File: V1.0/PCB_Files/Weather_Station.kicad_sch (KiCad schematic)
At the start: 45 parts, among them J1 N091-2832TSWFG02-H14, J2 USB_B_Micro, J3 Conn_01x04_Pin, J4 Conn_01x04_Pin, J5 Conn_01x06_Pin, U1 STM32F103C8T6, U2 HDC1080DMBR, U3 AMS1117-3.3, U5 SRV05-4, Y1 X322516MLB4SI

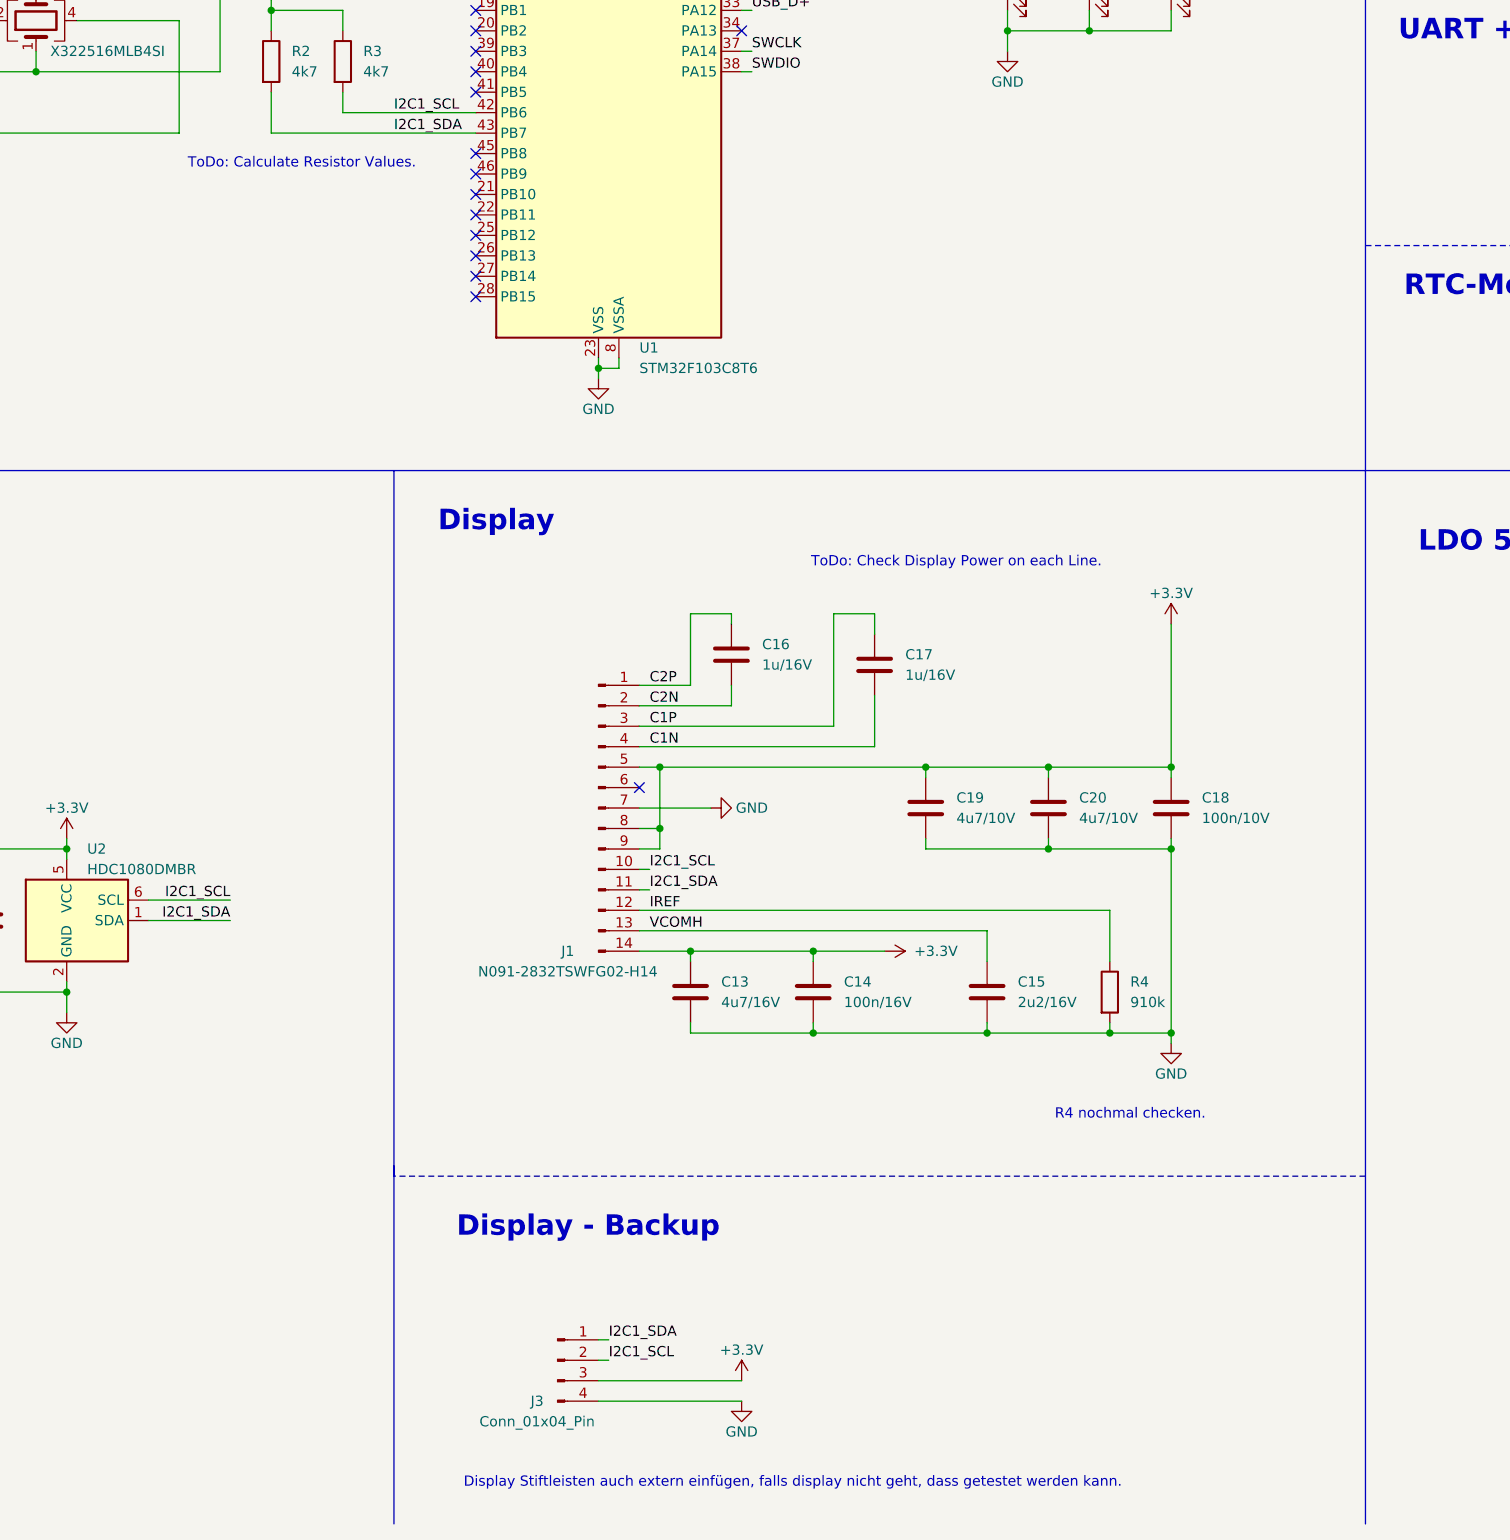
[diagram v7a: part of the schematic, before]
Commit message: Decided to not go with the display. Added Step file for display.
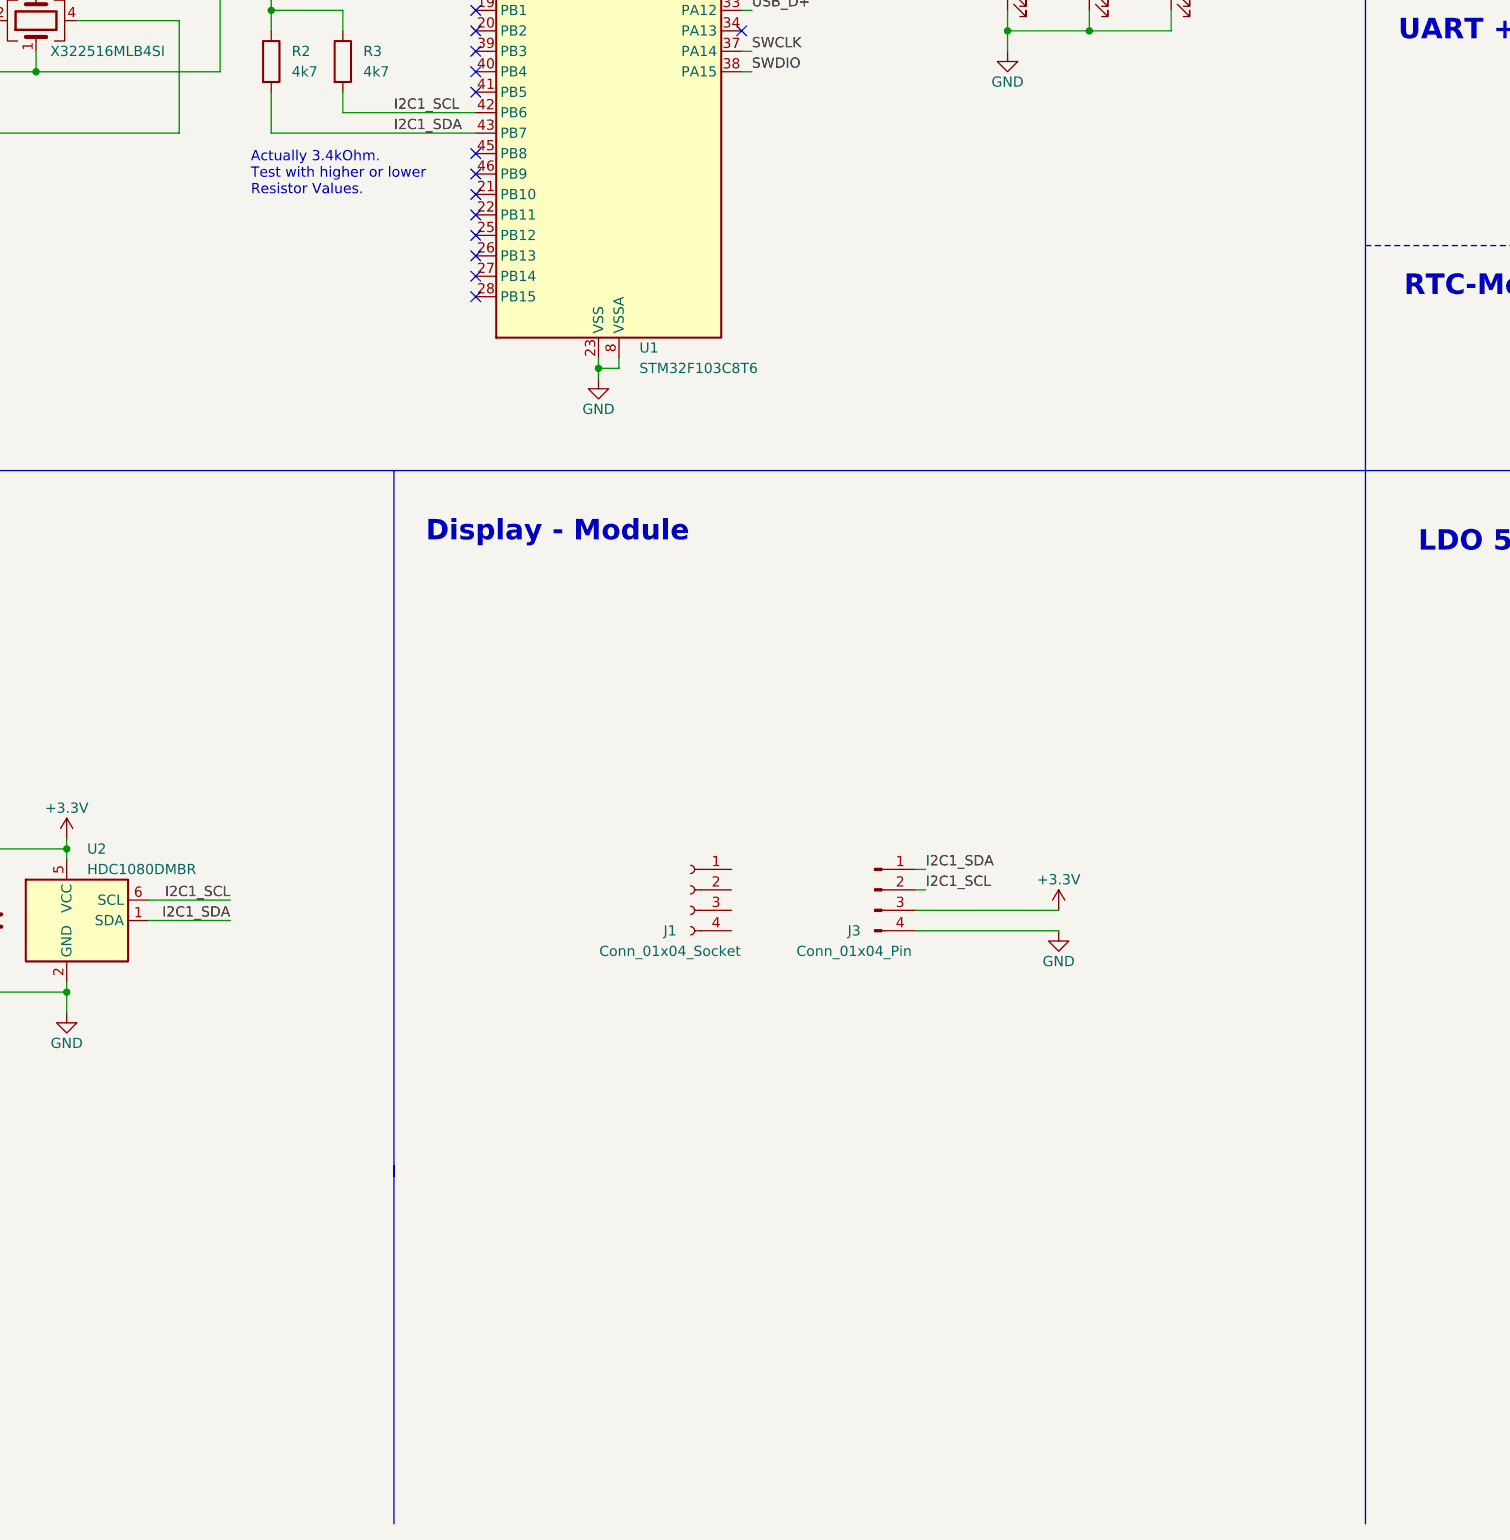
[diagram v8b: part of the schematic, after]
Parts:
- removed C13: 4u7/16V, Capacitor_SMD:C_0805_2012Metric, symbol Device:C
- removed C14: 100n/16V, Capacitor_SMD:C_0603_1608Metric, symbol Device:C
- removed C15: 2u2/16V, Capacitor_SMD:C_0805_2012Metric, symbol Device:C
- removed C16, C17: 1u/16V, Capacitor_SMD:C_0603_1608Metric, symbol Device:C
- removed C18: 100n/10V, Capacitor_SMD:C_0603_1608Metric, symbol Device:C
- removed C19, C20: 4u7/10V, Capacitor_SMD:C_0805_2012Metric, symbol Device:C
- removed J1: N091-2832TSWFG02-H14, Private_Connector_Display:OLED_SMD_128x32, symbol Connector:Conn_01x14_Pin
- removed R4: 910k, Resistor_SMD:R_0603_1608Metric, symbol Device:R
- added J1: Conn_01x04_Socket, Capacitor_SMD:C_0402_1005Metric, symbol Connector:Conn_01x04_Socket
- J3, J4: footprint Connector_PinHeader_1.00mm:PinHeader_1x04_P1.00mm_Vertical -> Connector_PinHeader_2.54mm:PinHeader_1x04_P2.54mm_Vertical
- J5: footprint Connector_PinHeader_1.00mm:PinHeader_1x06_P1.00mm_Vertical -> Connector_PinHeader_2.54mm:PinHeader_1x06_P2.54mm_Vertical
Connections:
- no-connect marks 26 -> 25
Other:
- note added: "Actually 3.4kOhm. Test with higher or lower Resistor Values."
- note added: "Display - Module"
- note removed: "Display"
- note removed: "Display - Backup"
- note removed: "Display Stiftleisten auch extern einfügen, falls display nicht geht, dass getestet werden kann."
- note removed: "R4 nochmal checken."
- note removed: "ToDo: Calculate Resistor Values."
- note removed: "ToDo: Check Display Power on each Line."
- moved on the sheet: J3
